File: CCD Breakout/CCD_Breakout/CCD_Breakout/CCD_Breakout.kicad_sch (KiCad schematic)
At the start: 0 parts

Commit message: CCD start
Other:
- added sheet CCD (ccd.kicad_sch)
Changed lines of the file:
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@@
 	(generator_version "9.0")
 	(paper "A4")
+	(sheet
+		(at 30.48 55.88)
+		(size 40.64 40.64)
+		(exclude_from_sim no)
+		(in_bom yes)
+		(on_board yes)
+		(dnp no)
+		(fields_autoplaced yes)
+		(stroke
+			(width 0.1524)
+			(type solid)
+		)
+		(fill
+			(color 0 0 0 0.0000)
+		)
+		(property "Sheetname" "CCD"
+			(at 30.48 55.1684 0)
+			(effects
+				(font
+					(size 1.27 1.27)
+				)
+				(justify left bottom)
+			)
+		)
+		(property "Sheetfile" "ccd.kicad_sch"
+			(at 30.48 97.1046 0)
+			(effects
+				(font
+					(size 1.27 1.27)
+				)
+				(justify left top)
+			)
+		)
+		(instances
+			(project "CCD_Breakout"
+				(path "/102965ac-29c6-4f96-94a4-d07431f6d693"
+					(page "2")
+				)
+			)
+		)
+	)
 	(sheet_instances
 		(path "/"

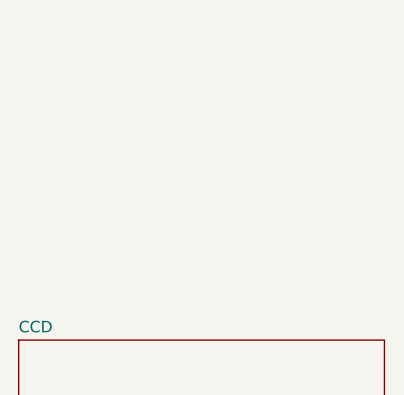
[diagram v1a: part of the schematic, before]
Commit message: Omp amp added
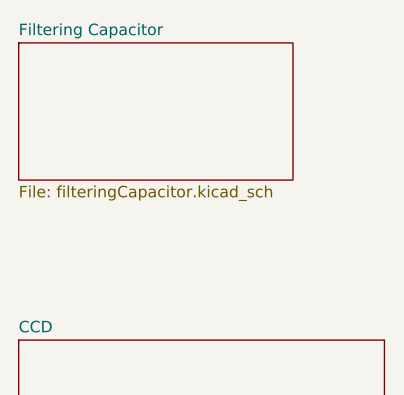
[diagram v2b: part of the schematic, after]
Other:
- added sheet Filtering Capacitor (filteringCapacitor.kicad_sch)
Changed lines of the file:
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@@
 	(paper "A4")
+	(sheet
+		(at 30.48 22.86)
+		(size 30.48 15.24)
+		(exclude_from_sim no)
+		(in_bom yes)
+		(on_board yes)
+		(dnp no)
+		(fields_autoplaced yes)
+		(stroke
+			(width 0.1524)
+			(type solid)
+		)
+		(fill
+			(color 0 0 0 0.0000)
+		)
+		(property "Sheetname" "Filtering Capacitor"
+			(at 30.48 22.1484 0)
+			(effects
+				(font
+					(size 1.27 1.27)
+				)
+				(justify left bottom)
+			)
+		)
+		(property "Sheetfile" "filteringCapacitor.kicad_sch"
+			(at 30.48 38.6846 0)
+			(effects
+				(font
+					(size 1.27 1.27)
+				)
+				(justify left top)
+			)
+		)
+		(instances
+			(project "CCD_Breakout"
+				(path "/102965ac-29c6-4f96-94a4-d07431f6d693"
+					(page "3")
+				)
+			)
+		)
+	)
 	(sheet
 		(at 30.48 55.88)

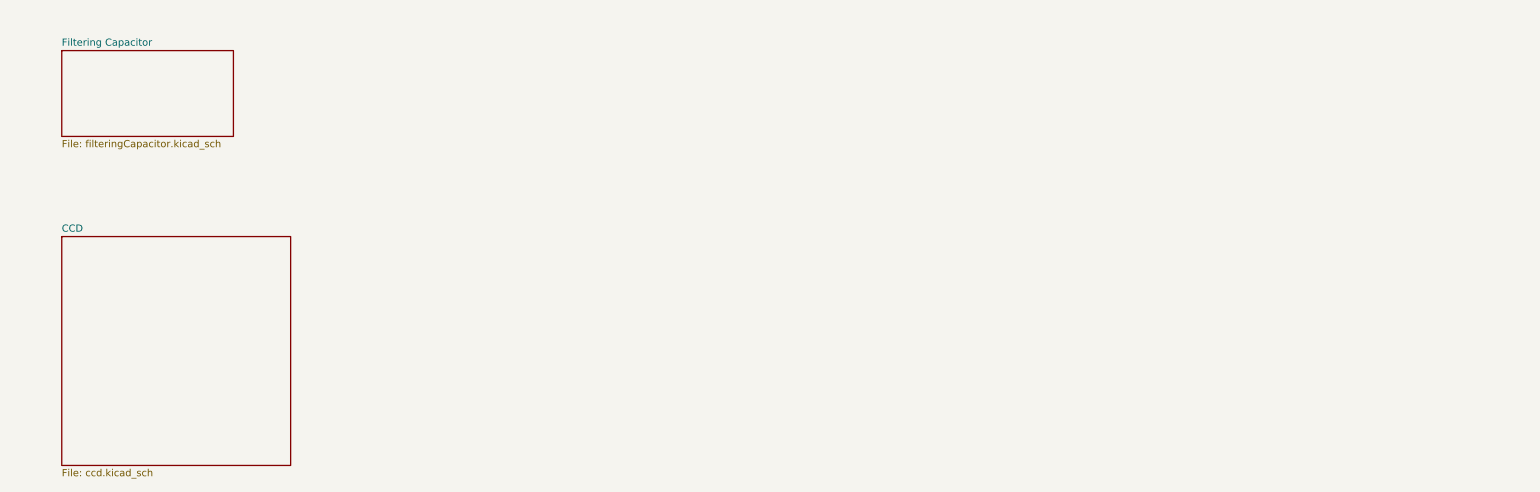
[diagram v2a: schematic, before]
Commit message: CCD Reorganization
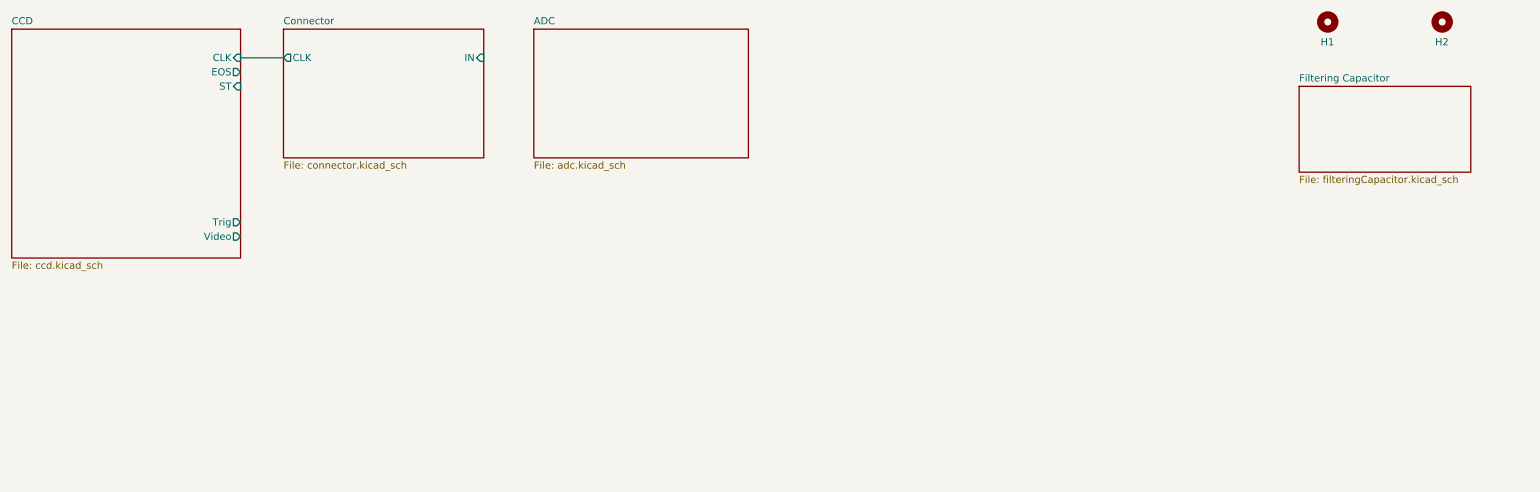
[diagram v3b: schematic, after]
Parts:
- added H1, H2: ~, symbol Mechanical:MountingHole
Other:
- added sheet ADC (adc.kicad_sch)
- added sheet Connector (connector.kicad_sch)
- sheet CCD ports: added CLK, EOS, ST, Trig, Video; removed none

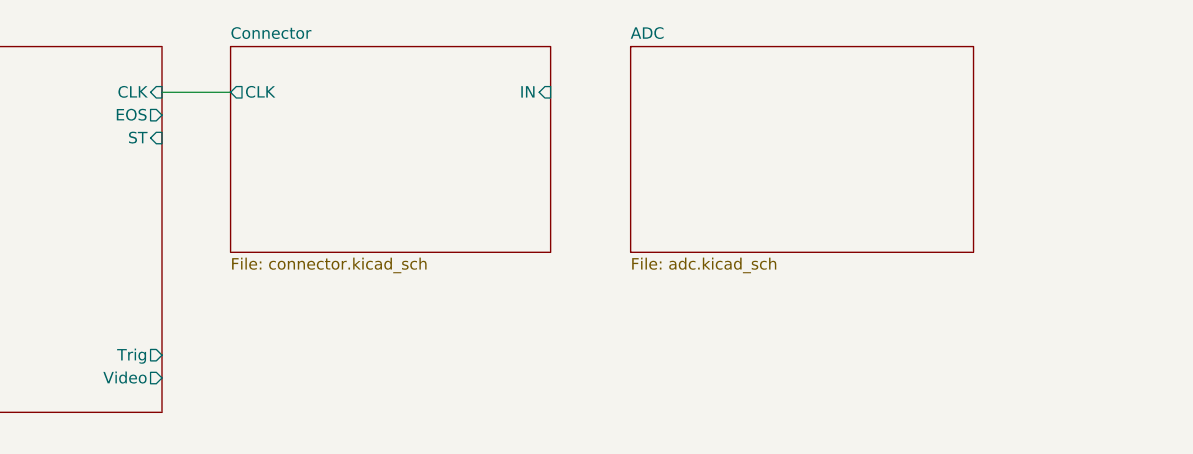
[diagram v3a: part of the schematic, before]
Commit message: Added Missing Resistors to CCD
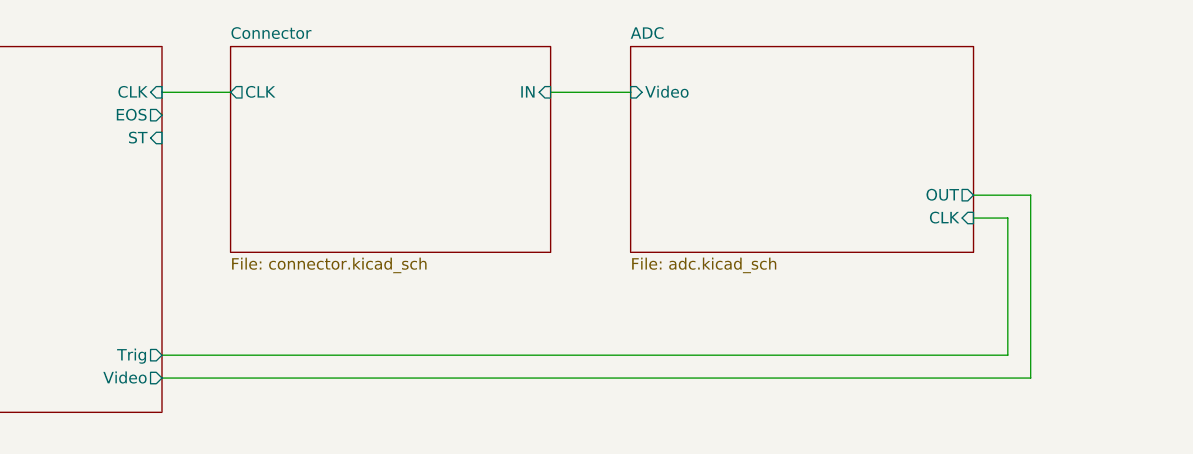
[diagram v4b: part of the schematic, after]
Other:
- sheet ADC ports: added CLK, OUT, Video; removed none
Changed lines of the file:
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@@
+	(wire
+		(pts
+			(xy 105.41 24.13) (xy 114.3 24.13)
+		)
+		(stroke
+			(width 0)
+			(type default)
+		)
+	)
+	(wire
+		(pts
+			(xy 156.21 53.34) (xy 156.21 38.1)
+		)
+		(stroke
+			(width 0)
+			(type default)
+		)
+	)
+	(wire
+		(pts
+			(xy 158.75 35.56) (xy 152.4 35.56)
+		)
+		(stroke
+			(width 0)
+			(type default)
+		)
+	)
+	(wire
+		(pts
+			(xy 158.75 55.88) (xy 158.75 35.56)
+		)
+		(stroke
+			(width 0)
+			(type default)
+		)
+	)
 	(wire
 		(pts
 			(xy 62.23 24.13) (xy 69.85 24.13)
+		)
+		(stroke
+			(width 0)
+			(type default)
+		)
+	)
+	(wire
+		(pts
+			(xy 62.23 55.88) (xy 158.75 55.88)
+		)
+		(stroke
+			(width 0)
+			(type default)
+		)
+	)
+	(wire
+		(pts
+			(xy 156.21 38.1) (xy 152.4 38.1)
+		)
+		(stroke
+			(width 0)
+			(type default)
+		)
+	)
+	(wire
+		(pts
+			(xy 62.23 53.34) (xy 156.21 53.34)
 		)
 		(stroke
@@
 			)
 		)
+		(pin "CLK" input
+			(at 152.4 38.1 0)
+			(effects
+				(font
+					(size 1.27 1.27)
+				)
+				(justify right)
+			)
+		)
+		(pin "OUT" output
+			(at 152.4 35.56 0)
+			(effects
+				(font
+					(size 1.27 1.27)
+				)
+				(justify right)
+			)
+		)
+		(pin "Video" input
+			(at 114.3 24.13 180)
+			(effects
+				(font
+					(size 1.27 1.27)
+				)
+				(justify left)
+			)
+		)

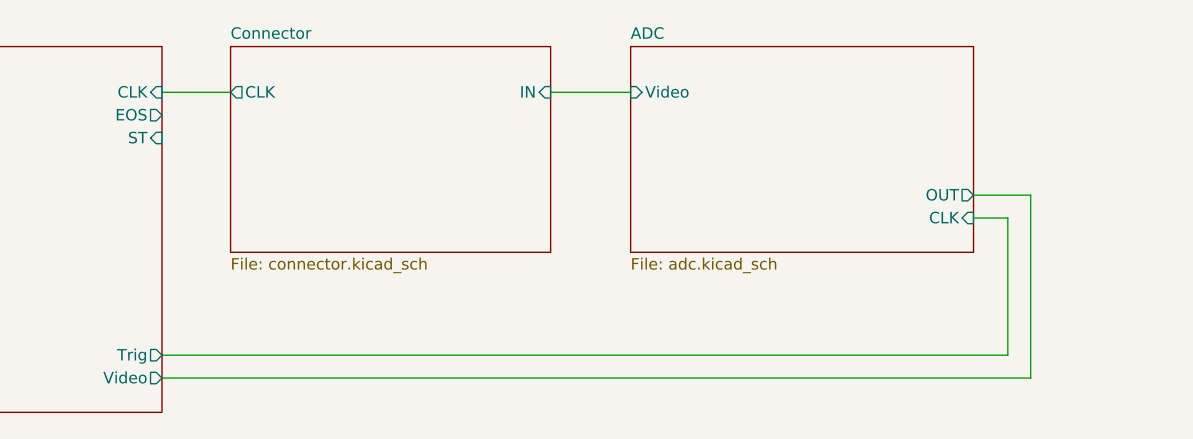
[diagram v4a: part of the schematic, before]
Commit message: ADC Changes + Delete Fan Connector
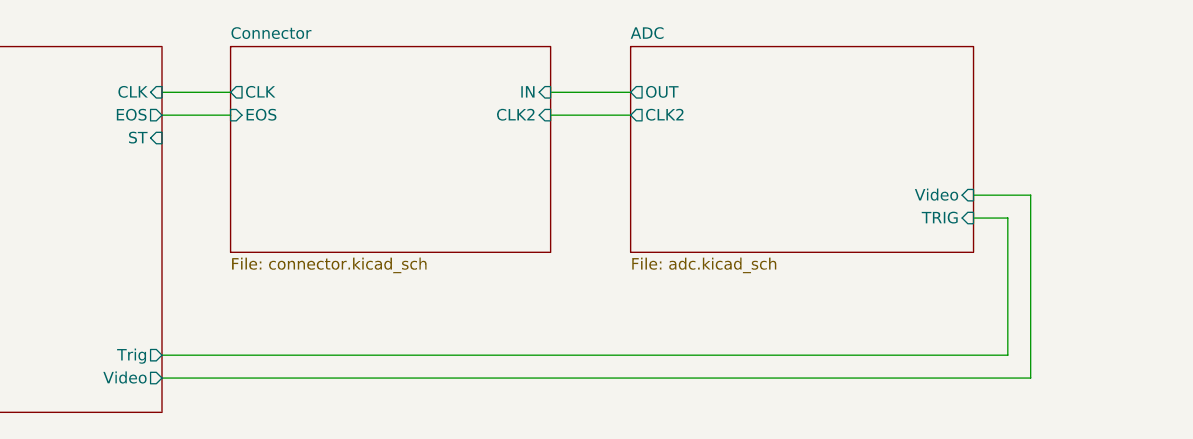
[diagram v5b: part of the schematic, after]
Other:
- sheet ADC ports: added CLK2, TRIG; removed CLK
- sheet Connector ports: added CLK2, EOS; removed none
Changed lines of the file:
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@@
+	(wire
+		(pts
+			(xy 105.41 26.67) (xy 114.3 26.67)
+		)
+		(stroke
+			(width 0)
+			(type default)
+		)
+	)
 	(wire
 		(pts
@@
 	(wire
 		(pts
-			(xy 158.75 35.56) (xy 152.4 35.56)
+			(xy 62.23 26.67) (xy 69.85 26.67)
+		)
+		(stroke
+			(width 0)
+			(type default)
+		)
+	)
+	(wire
+		(pts
+			(xy 152.4 35.56) (xy 158.75 35.56)
 		)
 		(stroke
@@
 			)
 		)
-		(pin "CLK" input
+		(pin "TRIG" input
 			(at 152.4 38.1 0)
 			(effects
@@
 		)
 		(pin "OUT" output
+			(at 114.3 24.13 180)
+			(effects
+				(font
+					(size 1.27 1.27)
+				)
+				(justify left)
+			)
+		)
+		(pin "Video" input
 			(at 152.4 35.56 0)
 			(effects
@@
 			)
 		)
-		(pin "Video" input
-			(at 114.3 24.13 180)
+		(pin "CLK2" output
+			(at 114.3 26.67 180)
 			(effects
 				(font
@@
 			(effects
 				(font
+					(size 1.27 1.27)
+				)
+				(justify right)
+			)
+		)
+		(pin "EOS" input
+			(at 69.85 26.67 180)
+			(effects
+				(font
+					(size 1.27 1.27)
+				)
+				(justify left)
+			)
+		)
+		(pin "CLK2" input
+			(at 105.41 26.67 0)
+			(effects
+				(font

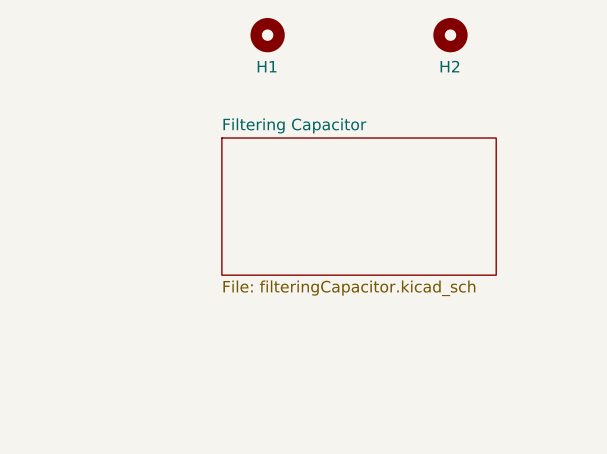
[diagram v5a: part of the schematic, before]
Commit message: Removed Unnecessary Filtering Capacitors
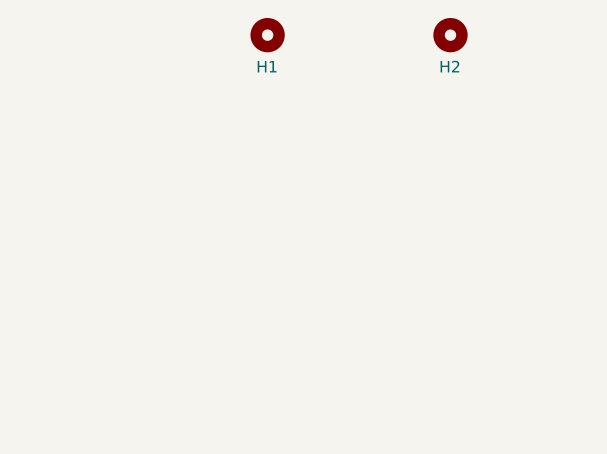
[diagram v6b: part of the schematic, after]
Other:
- removed sheet Filtering Capacitor
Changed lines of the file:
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@@
-	)
-	(sheet
-		(at 250.19 29.21)
-		(size 30.48 15.24)
-		(exclude_from_sim no)
-		(in_bom yes)
-		(on_board yes)
-		(dnp no)
-		(fields_autoplaced yes)
-		(stroke
-			(width 0.1524)
-			(type solid)
-		)
-		(fill
-			(color 0 0 0 0.0000)
-		)
-		(property "Sheetname" "Filtering Capacitor"
-			(at 250.19 28.4984 0)
-			(effects
-				(font
-					(size 1.27 1.27)
-				)
-				(justify left bottom)
-			)
-		)
-		(property "Sheetfile" "filteringCapacitor.kicad_sch"
-			(at 250.19 45.0346 0)
-			(effects
-				(font
-					(size 1.27 1.27)
-				)
-				(justify left top)
-			)
-		)
-		(instances
-			(project "CCD_Breakout"
-				(path "/102965ac-29c6-4f96-94a4-d07431f6d693"
-					(page "3")
-				)
-			)
-		)
 	)
 	(sheet

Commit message: OpAmp IC
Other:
- added sheet OP-AMP (opAmp.kicad_sch)
- sheet ADC ports: added opIND+, opIND-, opOUTD; removed none
- sheet CCD ports: added opINA+, opINA-, opINB+, opINB-, opINC+, opINC-, opOUTA, opOUTB, opOUTC; removed none

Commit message: ST and EOS Pin Connections
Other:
- sheet Connector ports: added ST; removed none
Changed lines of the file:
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@@
+	(wire
+		(pts
+			(xy 62.23 29.21) (xy 69.85 29.21)
+		)
+		(stroke
+			(width 0)
+			(type default)
+		)
+	)
 	(wire
 		(pts
@@
 			)
 		)
+		(pin "ST" output
+			(at 69.85 29.21 180)
+			(effects
+				(font
+					(size 1.27 1.27)
+				)
+				(justify left)
+			)
+		)
